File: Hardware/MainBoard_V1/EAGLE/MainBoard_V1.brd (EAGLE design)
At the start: 94 x 54 mm, 43 parts, among them IC1 REG1117, J1 NANO_FOOTPRINTNANO, J4 I2C, K1 RELAY-SPDT-JZC-11F, Q2 600mA/40V, Q3 600mA/40V, U1 MOC3021M, U4 MCT2EM, X2 AC

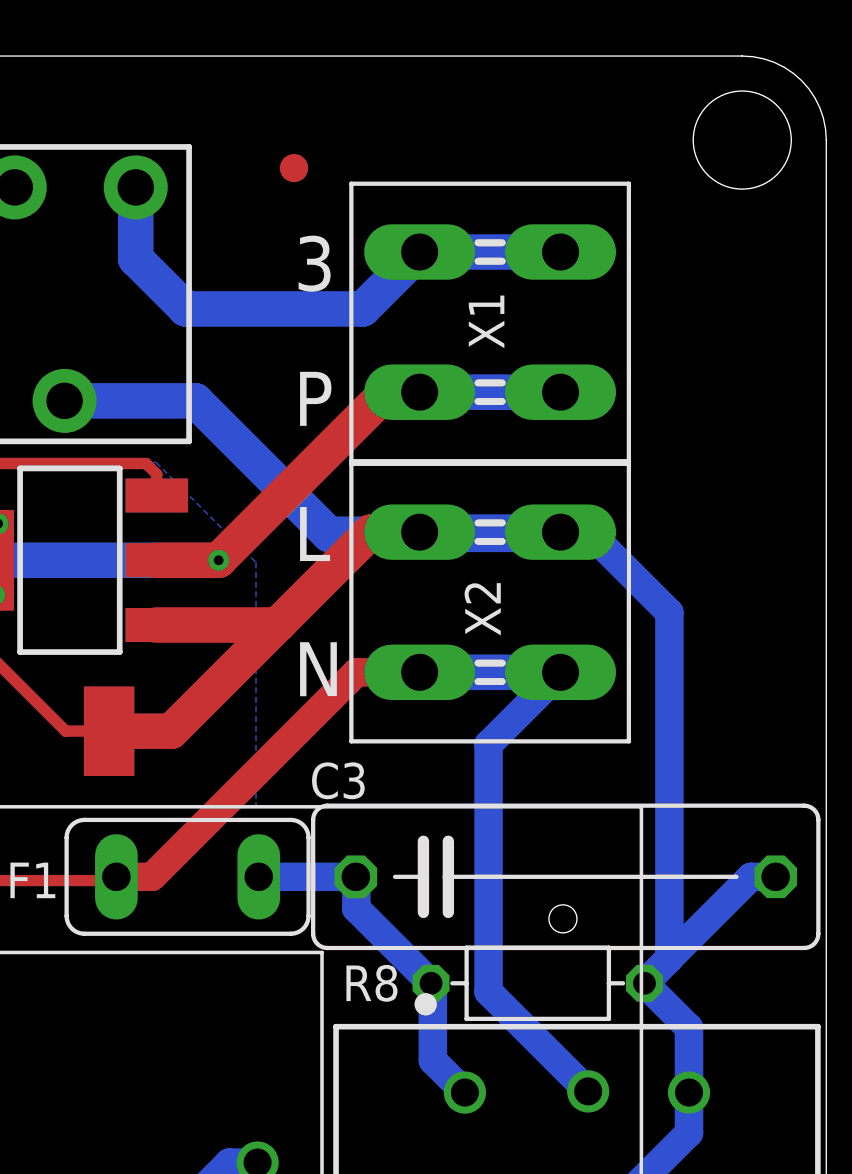
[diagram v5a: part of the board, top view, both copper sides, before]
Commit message: Spade connectors BOM fix
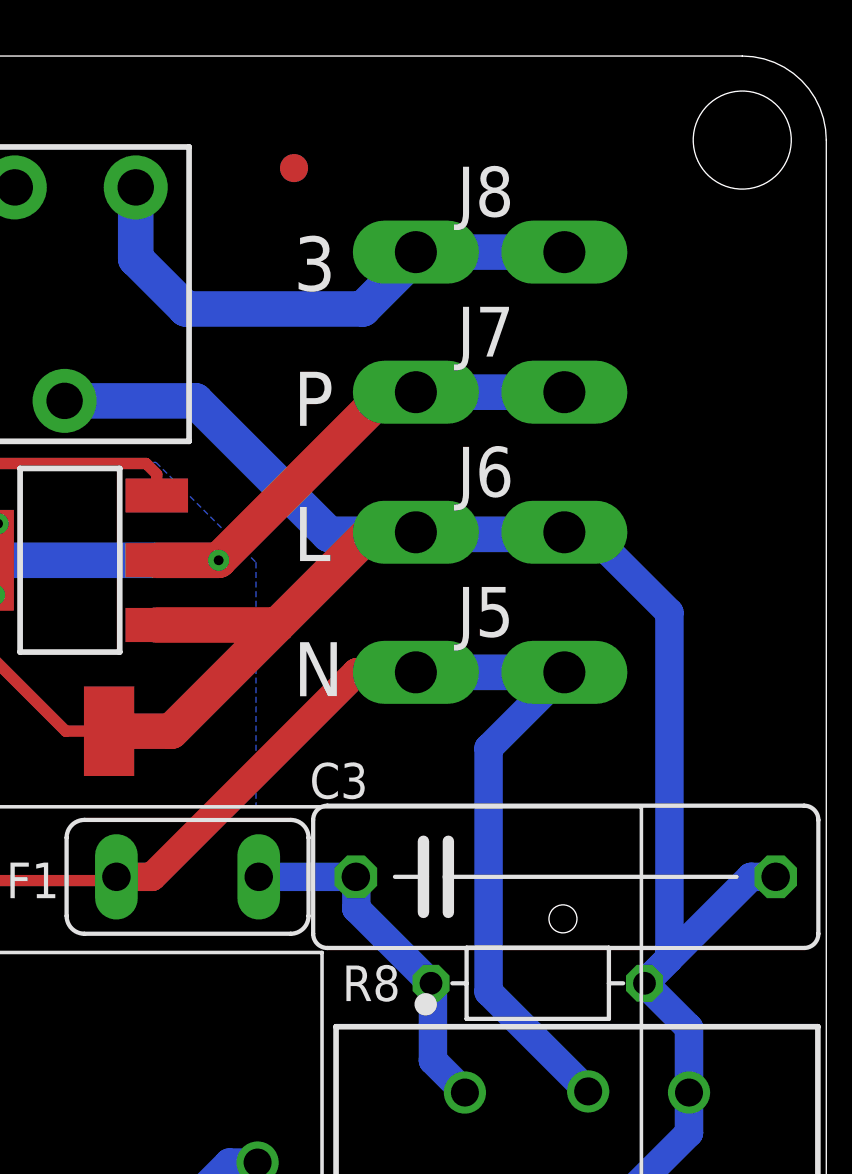
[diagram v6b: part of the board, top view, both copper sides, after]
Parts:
- removed X1: (no value), con-rib:SH5-2
- removed X2: AC, con-rib:SH5-2
- added J5, J6, J7, J8: (no value), con-faston:62409-1
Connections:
- net 3WAYVALVE: now also J8.A1, J8.A2; no longer X1.3, X1.4
- net ACL: now also J6.A1, J6.A2; no longer X2.3, X2.4
- net ACN: now also J5.A1, J5.A2; no longer X2.1, X2.2
- net PUMP: now also J7.A1, J7.A2; no longer X1.1, X1.2
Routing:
- net ACL: track 92.8 -> 87.5 mm
